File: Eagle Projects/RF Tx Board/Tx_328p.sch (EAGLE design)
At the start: 45 parts, among them Q3 16MHz, Q4 16MHz, U1 ATMEGA328P_TQFP, U2 MCP2551, X1 5566-6, X2 5566-6

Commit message: Sorted Matts Board :)
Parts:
- removed ., .., R1, R3: 1k, rcl:R-US_M0805
- removed RX_3DR_LED, RX_LED, TX_LED, TX_LED_GPS: (no value), led:LEDCHIP-LED0805
- removed S1: SKHMPSE010, switch:SKHMPSE010
- removed USART: (no value), pinhead:PINHD-1X2
- added C10, C9: 22pF, resistor:C-EUC0805K
- added JP1: (no value), pinhead:PINHD-1X2
- added U$4: HEADER-2WAY, con-TE-EP:HEADER-2WAY
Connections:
- removed net +5V: R7.1
- removed net N$20: X1-5.S
- removed net N$21: X1-6.S
- removed net N$26: X2-5.S
- removed net N$27: X2-6.S
- removed net N$3: R2.2, U1.PC6(/RESET)
- removed net N$4: R3.1, TX_LED_GPS.C
- removed net N$5: R1.1, RX_3DR_LED.C
- removed net N$6: ...1, RX_LED.C
- removed net N$8: ..1, TX_LED.C
- removed net N$9: C4.1, U1.AGND, U1.GND@3, U1.GND@5
- new net N$17: ISP1.VCC, JP1.2
- new net SPARE1: X1-5.S, X2-5.S
- new net SPARE2: X1-6.S, X2-6.S
- net GND: now also C10.2, C9.2, U1.AGND, U1.GND@3, U1.GND@5; no longer ...2, ..2, R1.2, R3.2, S1.1.1, S1.1.2
- net N$1: now also C9.1, Q1.2, Q2.2; no longer Q1.1, Q2.1
- net N$2: now also C10.1, Q1.1, Q2.1; no longer Q1.2, Q2.2
- net RST: now also R2.2, RESET.3, RESET.4, U1.PC6(/RESET)
- net RX0: now also U$4.P$1; no longer TX_LED.A, TX_LED_GPS.A, USART.2
- net TX0: now also U$4.P$2; no longer RX_3DR_LED.A, RX_LED.A, USART.1
- net VCC: now also C4.1, JP1.1, R7.1, U1.VCC@6; no longer ISP1.VCC, RESET.3, RESET.4, S1.2.1, S1.2.2
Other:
- moved on the sheet: C4, Q1, Q2

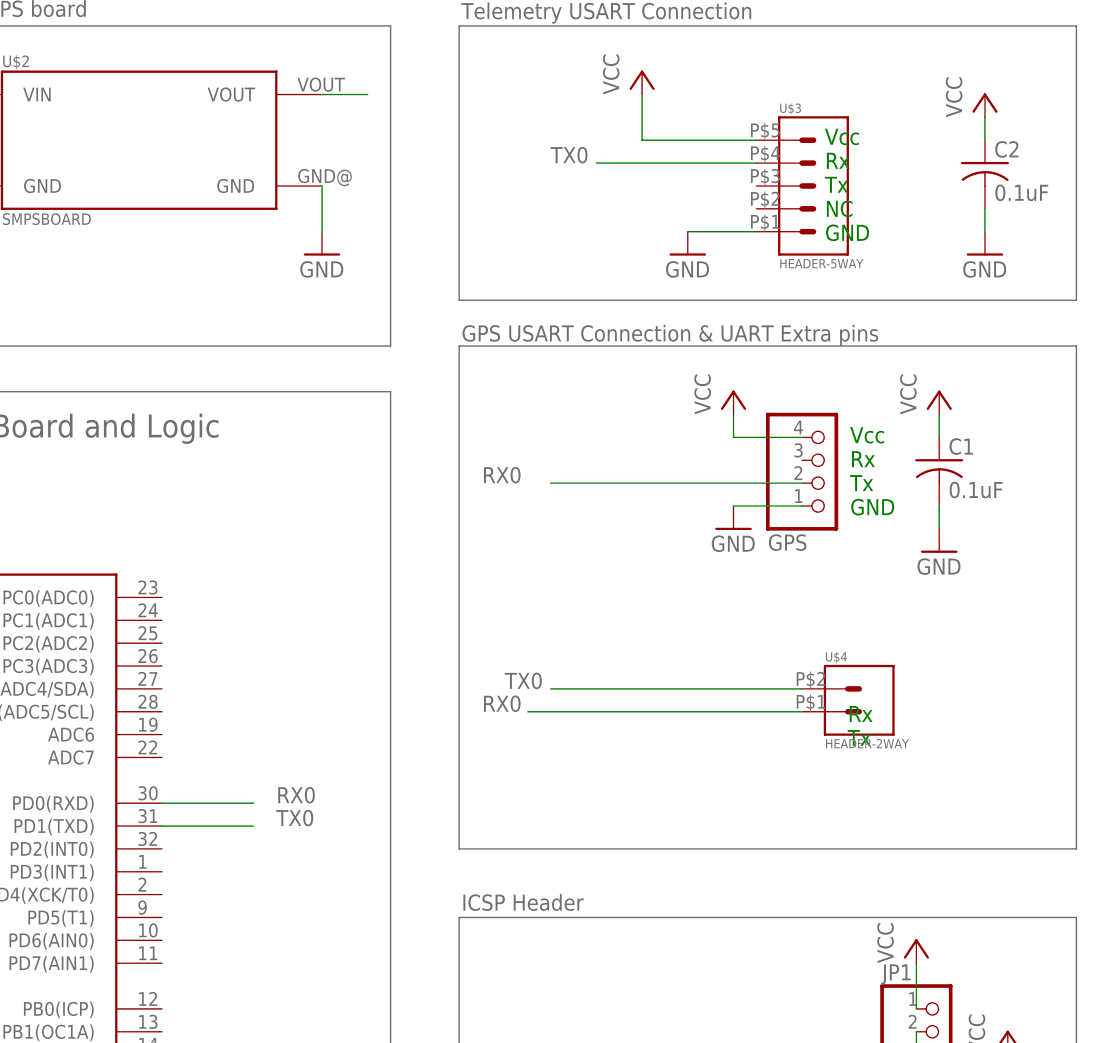
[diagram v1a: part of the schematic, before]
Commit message: Added status LEDs for Tx board
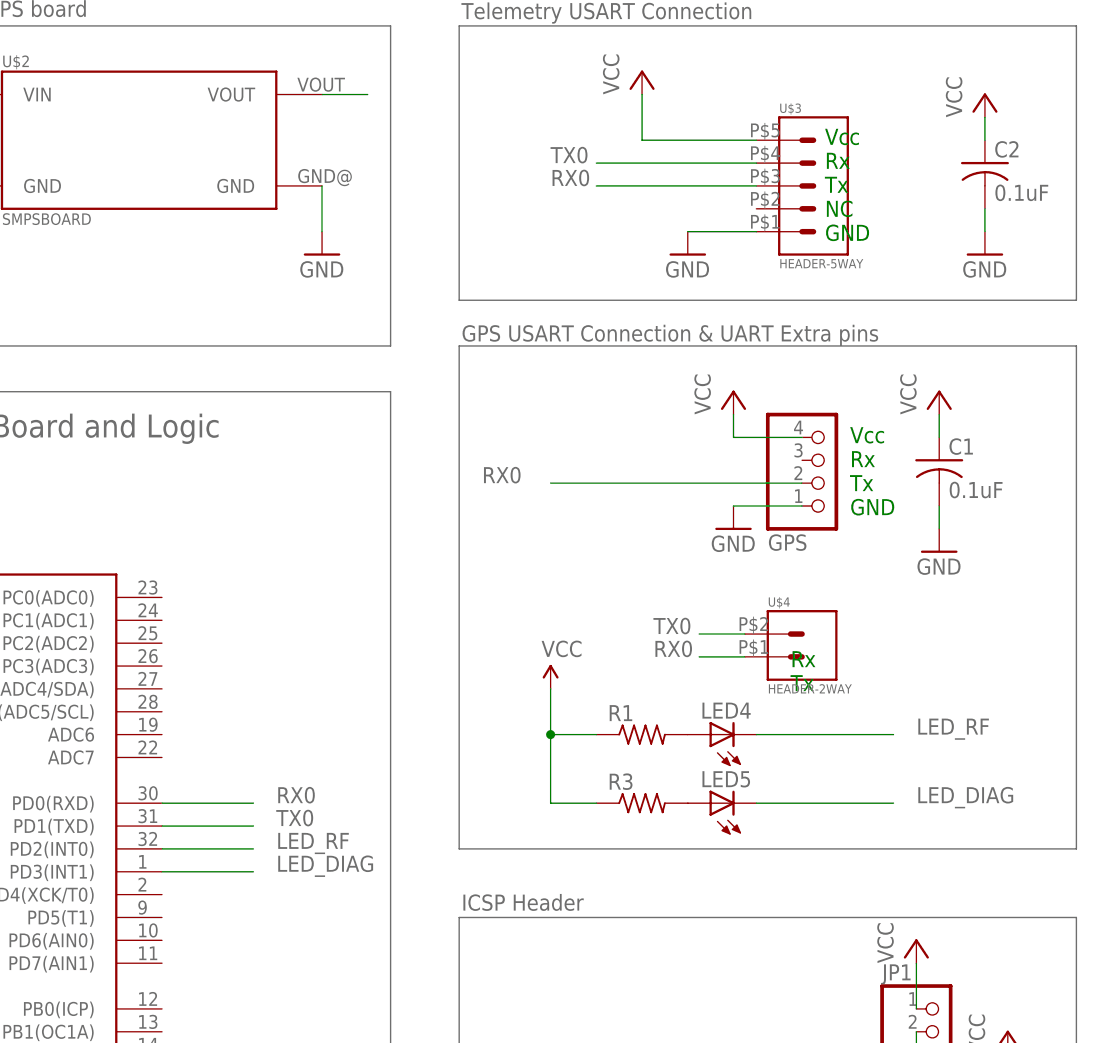
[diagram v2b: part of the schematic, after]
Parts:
- added LED4, LED5: (no value), led:LEDSML0805
- added R1, R3: (no value), resistor:R-US_M0805
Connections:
- new net LED_DIAG: LED5.C, U1.PD3(INT1)
- new net LED_RF: LED4.C, U1.PD2(INT0)
- new net N$4: LED4.A, R1.2
- new net N$5: LED5.A, R3.2
- net RX0: now also U$3.P$3
- net VCC: now also R1.1, R3.1
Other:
- moved on the sheet: U$4
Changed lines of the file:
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@@
 <part name="P+12" library="supply1" deviceset="VCC" device=""/>
 <part name="U$4" library="con-TE-EP" deviceset="HEADER-2WAY" device=""/>
+<part name="LED4" library="led" deviceset="LED" device="SML0805"/>
+<part name="LED5" library="led" deviceset="LED" device="SML0805"/>
+<part name="R1" library="resistor" deviceset="R-US_" device="M0805"/>
+<part name="R3" library="resistor" deviceset="R-US_" device="M0805"/>
+<part name="SUPPLY1" library="SparkFun-Aesthetics" deviceset="VCC" device=""/>
 </parts>
 <sheets>
@@
 Tx
 GND</text>
-<text x="195.58" y="74.93" size="1.778" layer="91">
+<text x="189.23" y="81.026" size="1.778" layer="91">
 Rx
 Tx
@@
 <instance part="GND18" gate="1" x="30.48" y="48.26"/>
 <instance part="P+12" gate="VCC" x="55.88" y="55.88"/>
-<instance part="U$4" gate="G$1" x="195.58" y="81.28"/>
+<instance part="U$4" gate="G$1" x="189.23" y="87.376"/>
+<instance part="LED4" gate="G$1" x="180.34" y="76.2" rot="R90"/>
+<instance part="LED5" gate="G$1" x="180.34" y="68.58" rot="R90"/>
+<instance part="R1" gate="G$1" x="172.72" y="76.2"/>
+<instance part="R3" gate="G$1" x="172.72" y="68.58"/>
+<instance part="SUPPLY1" gate="G$1" x="162.56" y="81.28"/>
 </instances>
 <busses>
@@
 <wire x1="55.88" y1="53.34" x2="55.88" y2="50.8" width="0.1524" layer="91"/>
 </segment>
+<segment>
+<pinref part="R1" gate="G$1" pin="1"/>
+<wire x1="167.64" y1="76.2" x2="162.56" y2="76.2" width="0.1524" layer="91"/>
+<wire x1="162.56" y1="76.2" x2="162.56" y2="81.28" width="0.1524" layer="91"/>
+<pinref part="R3" gate="G$1" pin="1"/>
+<wire x1="167.64" y1="68.58" x2="162.56" y2="68.58" width="0.1524" layer="91"/>
+<wire x1="162.56" y1="68.58" x2="162.56" y2="76.2" width="0.1524" layer="91"/>
+<pinref part="SUPPLY1" gate="G$1" pin="VCC"/>
+<junction x="162.56" y="76.2"/>
+</segment>
 </net>
 <net name="TX0" class="0">
@@
 </segment>
 <segment>
-<label x="157.48" y="81.28" size="1.778" layer="95"/>
-<wire x1="190.5" y1="81.28" x2="162.56" y2="81.28" width="0.1524" layer="91"/>
+<label x="173.99" y="87.376" size="1.778" layer="95"/>
+<wire x1="184.15" y1="87.376" x2="179.07" y2="87.376" width="0.1524" layer="91"/>
 <pinref part="U$4" gate="G$1" pin="P$2"/>
 </segment>
@@
 </segment>
 <segment>
-<label x="154.94" y="78.74" size="1.778" layer="95"/>
-<wire x1="190.5" y1="78.74" x2="160.02" y2="78.74" width="0.1524" layer="91"/>
+<label x="173.99" y="84.836" size="1.778" layer="95"/>
+<wire x1="184.15" y1="84.836" x2="179.07" y2="84.836" width="0.1524" layer="91"/>
 <pinref part="U$4" gate="G$1" pin="P$1"/>
 </segment>
@@
 <label x="154.94" y="104.14" size="1.778" layer="95"/>
 <wire x1="162.56" y1="104.14" x2="190.5" y2="104.14" width="0.1524" layer="91"/>
+</segment>
+<segment>
+<pinref part="U$3" gate="G$1" pin="P$3"/>
+<wire x1="185.42" y1="137.16" x2="167.64" y2="137.16" width="0.1524" layer="91"/>
+<label x="162.56" y="137.16" size="1.778" layer="95"/>
 </segment>
 </net>
@@
 </segment>
 </net>
+<net name="LED_DIAG" class="0">
+<segment>
+<pinref part="U1" gate="U$1" pin="PD3(INT1)"/>
+<wire x1="119.38" y1="60.96" x2="129.54" y2="60.96" width="0.1524" layer="91"/>
+<label x="132.08" y="60.96" size="1.778" layer="95"/>
+</segment>
+<segment>
+<pinref part="LED5" gate="G$1" pin="C"/>
+<wire x1="185.42" y1="68.58" x2="200.66" y2="68.58" width="0.1524" layer="91"/>
+<label x="203.2" y="68.58" size="1.778" layer="95"/>
+</segment>
+</net>
+<net name="LED_RF" class="0">
+<segment>
+<pinref part="U1" gate="U$1" pin="PD2(INT0)"/>
+<wire x1="119.38" y1="63.5" x2="129.54" y2="63.5" width="0.1524" layer="91"/>
+<label x="132.08" y="63.5" size="1.778" layer="95"/>
+</segment>
+<segment>
+<pinref part="LED4" gate="G$1" pin="C"/>
+<wire x1="185.42" y1="76.2" x2="200.66" y2="76.2" width="0.1524" layer="91"/>
+<label x="203.2" y="76.2" size="1.778" layer="95"/>
+</segment>
+</net>
+<net name="N$4" class="0">
+<segment>
+<pinref part="LED4" gate="G$1" pin="A"/>
+<pinref part="R1" gate="G$1" pin="2"/>
+</segment>
+</net>
+<net name="N$5" class="0">
+<segment>
+<pinref part="LED5" gate="G$1" pin="A"/>
+<pinref part="R3" gate="G$1" pin="2"/>
+</segment>
+</net>

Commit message: Exported BMP's
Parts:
- added JP2: (no value), pinhead:PINHD-1X1
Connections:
- new net N$3: GPS.3, JP2.1
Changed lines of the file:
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@@
 <part name="R3" library="resistor" deviceset="R-US_" device="M0805"/>
 <part name="SUPPLY1" library="SparkFun-Aesthetics" deviceset="VCC" device=""/>
+<part name="JP2" library="pinhead" deviceset="PINHD-1X1" device=""/>
 </parts>
 <sheets>
@@
 <instance part="R3" gate="G$1" x="172.72" y="68.58"/>
 <instance part="SUPPLY1" gate="G$1" x="162.56" y="81.28"/>
+<instance part="JP2" gate="G$1" x="170.18" y="106.68" rot="R180"/>
 </instances>
 <busses>
@@
 </segment>
 </net>
+<net name="N$3" class="0">
+<segment>
+<pinref part="GPS" gate="A" pin="3"/>
+<pinref part="JP2" gate="G$1" pin="1"/>
+<wire x1="190.5" y1="106.68" x2="172.72" y2="106.68" width="0.1524" layer="91"/>
+</segment>
+</net>

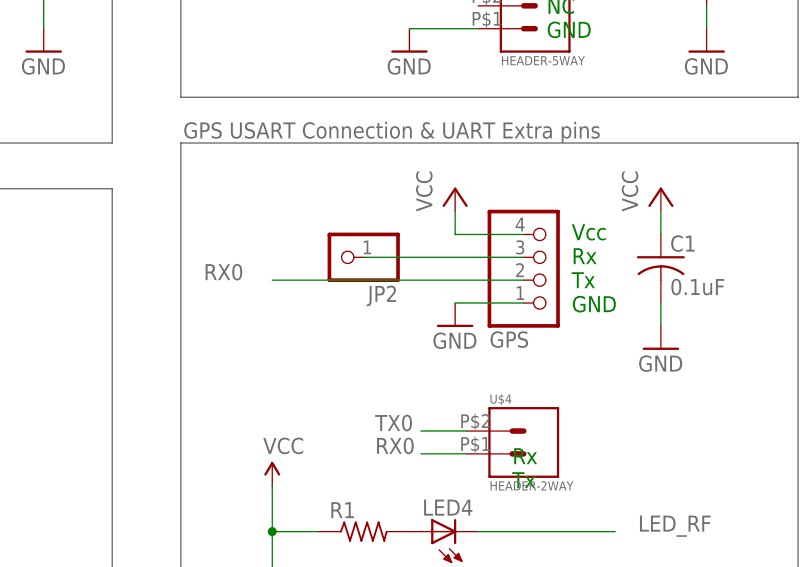
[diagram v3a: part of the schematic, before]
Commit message: Fixed n00b mistake on board+Schematic for Tx board
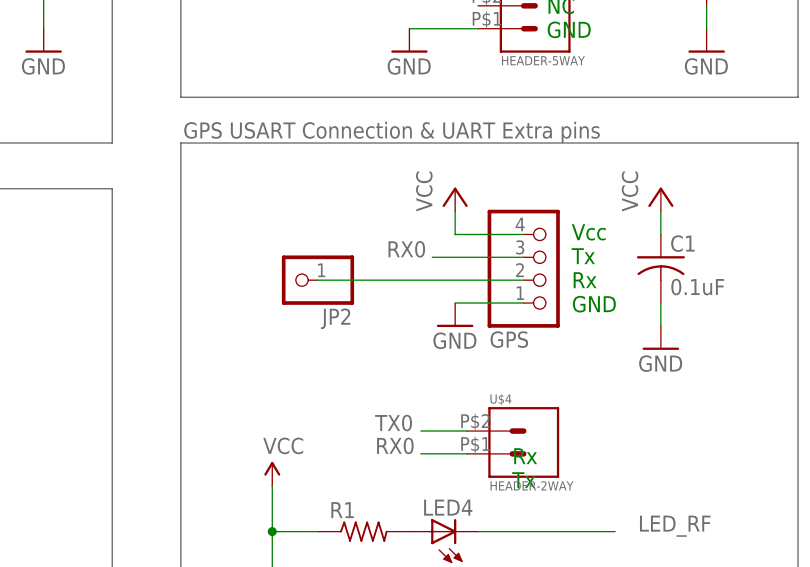
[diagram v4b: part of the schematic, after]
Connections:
- net N$3: now also GPS.2; no longer GPS.3
- net RX0: now also GPS.3; no longer GPS.2
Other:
- note added: "Vcc Tx Rx GND"
- note removed: "Vcc Rx Tx GND"
- moved on the sheet: JP2
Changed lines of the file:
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@@
 GND</text>
 <text x="195.834" y="100.584" size="1.778" layer="91">Vcc
+Tx
 Rx
-Tx
 GND</text>
 <text x="189.23" y="81.026" size="1.778" layer="91">
@@
 <instance part="R3" gate="G$1" x="172.72" y="68.58"/>
 <instance part="SUPPLY1" gate="G$1" x="162.56" y="81.28"/>
-<instance part="JP2" gate="G$1" x="170.18" y="106.68" rot="R180"/>
+<instance part="JP2" gate="G$1" x="165.1" y="104.14" rot="R180"/>
 </instances>
 <busses>
@@
 </segment>
 <segment>
-<pinref part="GPS" gate="A" pin="2"/>
-<label x="154.94" y="104.14" size="1.778" layer="95"/>
-<wire x1="162.56" y1="104.14" x2="190.5" y2="104.14" width="0.1524" layer="91"/>
-</segment>
-<segment>
 <pinref part="U$3" gate="G$1" pin="P$3"/>
 <wire x1="185.42" y1="137.16" x2="167.64" y2="137.16" width="0.1524" layer="91"/>
 <label x="162.56" y="137.16" size="1.778" layer="95"/>
+</segment>
+<segment>
+<pinref part="GPS" gate="A" pin="3"/>
+<wire x1="190.5" y1="106.68" x2="180.34" y2="106.68" width="0.1524" layer="91"/>
+<label x="175.26" y="106.68" size="1.778" layer="95"/>
 </segment>
 </net>
@@
 <net name="N$3" class="0">
 <segment>
-<pinref part="GPS" gate="A" pin="3"/>
+<pinref part="GPS" gate="A" pin="2"/>
+<wire x1="190.5" y1="104.14" x2="167.64" y2="104.14" width="0.1524" layer="91"/>
 <pinref part="JP2" gate="G$1" pin="1"/>
-<wire x1="190.5" y1="106.68" x2="172.72" y2="106.68" width="0.1524" layer="91"/>
-</segment>
-</net>
+</segment>
+</net>

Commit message: Fixed my silly on matts board
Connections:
- net CANCS: now also U1.PB2(SS/OC1B)
- net CANINT: now also U1.PB1(OC1A)
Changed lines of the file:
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@@
 <junction x="114.3" y="-58.42"/>
+</segment>
+<segment>
+<pinref part="U1" gate="U$1" pin="PB1(OC1A)"/>
+<wire x1="119.38" y1="43.18" x2="129.54" y2="43.18" width="0.1524" layer="91"/>
+<label x="132.08" y="43.18" size="1.778" layer="95"/>
 </segment>
 </net>
@@
 <label x="50.8" y="-45.72" size="1.778" layer="95"/>
 </segment>
+<segment>
+<pinref part="U1" gate="U$1" pin="PB2(SS/OC1B)"/>
+<wire x1="119.38" y1="40.64" x2="129.54" y2="40.64" width="0.1524" layer="91"/>
+<label x="132.08" y="40.64" size="1.778" layer="95"/>
+</segment>
 </net>
